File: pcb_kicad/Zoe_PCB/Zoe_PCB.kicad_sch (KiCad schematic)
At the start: 13 parts, among them U2 J2

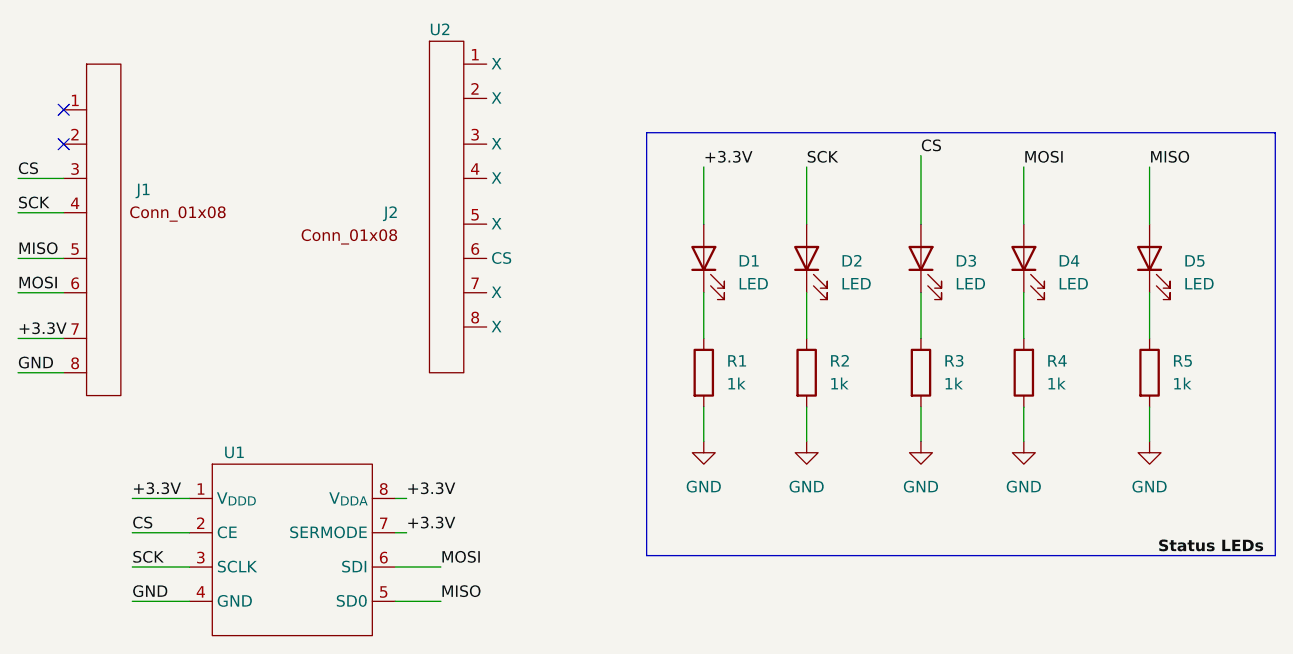
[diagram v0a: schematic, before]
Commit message: Added new DS1722 Footprint
Created new footprint for the DS1722
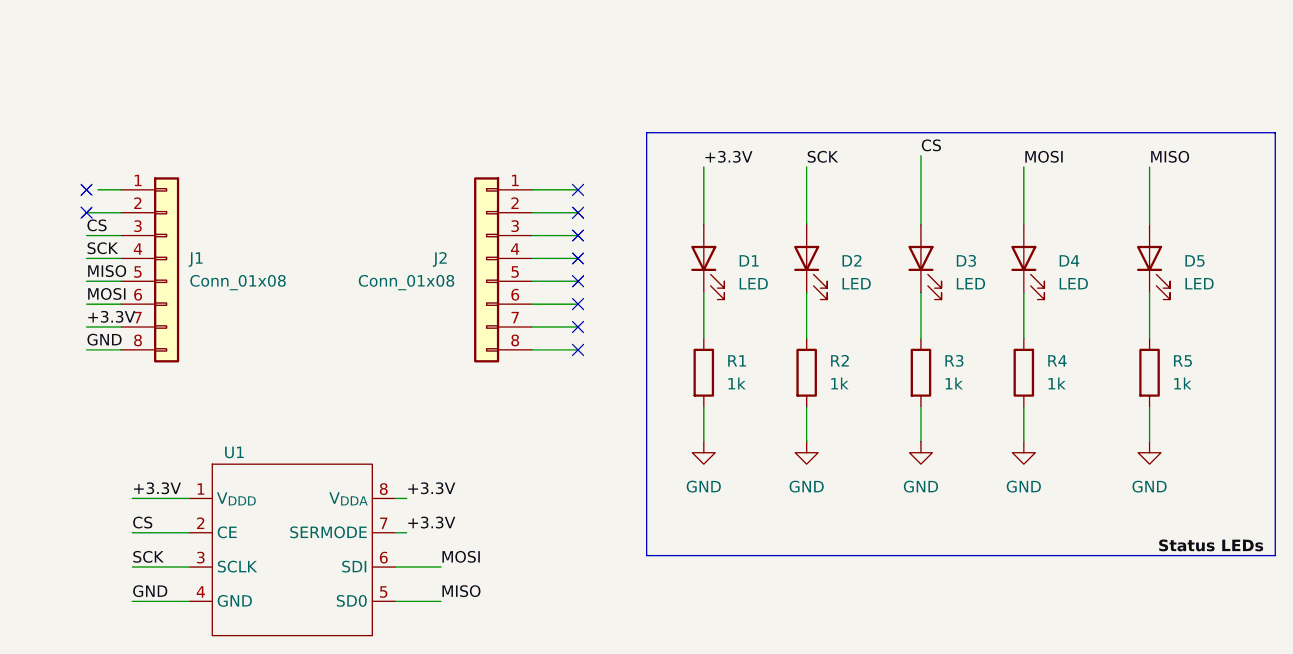
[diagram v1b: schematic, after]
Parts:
- removed J1: ~, symbol Jumper:J1
- removed U2: J2, symbol Jumper:J2
- added J1, J2: Conn_01x08, Connector_PinHeader_2.54mm:PinHeader_1x08_P2.54mm_Vertical, symbol Connector_Generic:Conn_01x08
- D1, D2, D3, D4, D5: footprint (none) -> LED_SMD:LED_0805_2012Metric
- R1, R2, R3, R4, R5: footprint (none) -> Resistor_SMD:R_0805_2012Metric
- U1: footprint (none) -> Zoe_PCB:Zoe_DS1722
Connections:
- net +3.3V: now also J1.7 (Pin_7)
- net CS: now also J1.3 (Pin_3)
- net GND: now also J1.8 (Pin_8)
- net MISO: now also J1.5 (Pin_5)
- net MOSI: now also J1.6 (Pin_6)
- net SCK: now also J1.4 (Pin_4)
- no-connect marks 2 -> 10

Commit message: Finished PCB board and confirmed readouts of motor
Finished programming PCB chip, also started checking the frequency of the motor in lab, and it appears to be correct :) -- need to add additional algorithms for excellence.
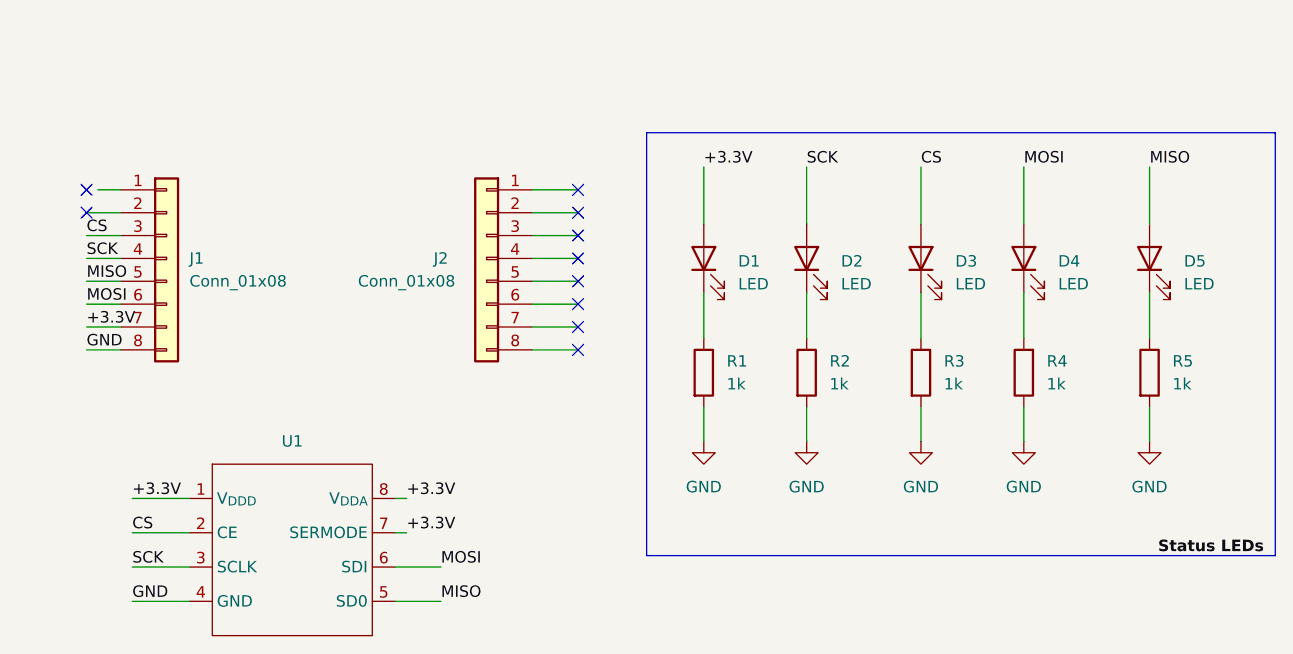
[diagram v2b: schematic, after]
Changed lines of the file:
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@@
     (stroke (width 0) (type default))
   )
-  (wire (pts (xy 195.58 60.96) (xy 195.58 68.58))
+  (wire (pts (xy 195.58 62.23) (xy 195.58 68.58))
     (stroke (width 0) (type default))
   )
@@
     (effects (font (size 1.27 1.27)) (justify left bottom))
   )
-  (label "CS" (at 195.58 60.96 0) (fields_autoplaced)
-    (effects (font (size 1.27 1.27)) (justify left bottom))
-    (property "CS" "" (at 195.58 62.23 0)
+  (label "CS" (at 195.58 62.23 0) (fields_autoplaced)
+    (effects (font (size 1.27 1.27)) (justify left bottom))
+    (property "CS" "" (at 195.58 63.5 0)
       (effects (font (size 1.27 1.27) italic) (justify left))
     )
@@
   (symbol (lib_id "Zoe_PCB:DS1722") (at 125.73 104.14 0) (unit 1)
     (in_bom yes) (on_board yes) (dnp no) (fields_autoplaced)
-    (property "Reference" "U1" (at 118.11 93.98 0)
-      (effects (font (size 1.27 1.27)) (justify left))
+    (property "Reference" "U1" (at 125.73 92.71 0)
+      (effects (font (size 1.27 1.27)))
     )
     (property "Value" "~" (at 128.27 95.25 0)
